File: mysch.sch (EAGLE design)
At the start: 41 parts, among them IC1 CY8C4247LQI-BL483, IC2 74HC595N, J1 FTSH-105-01-L-DV-K, J2 22-23-2051, Q1 RFD3055LE, Y2 ECS-240-8-36CKM-TR

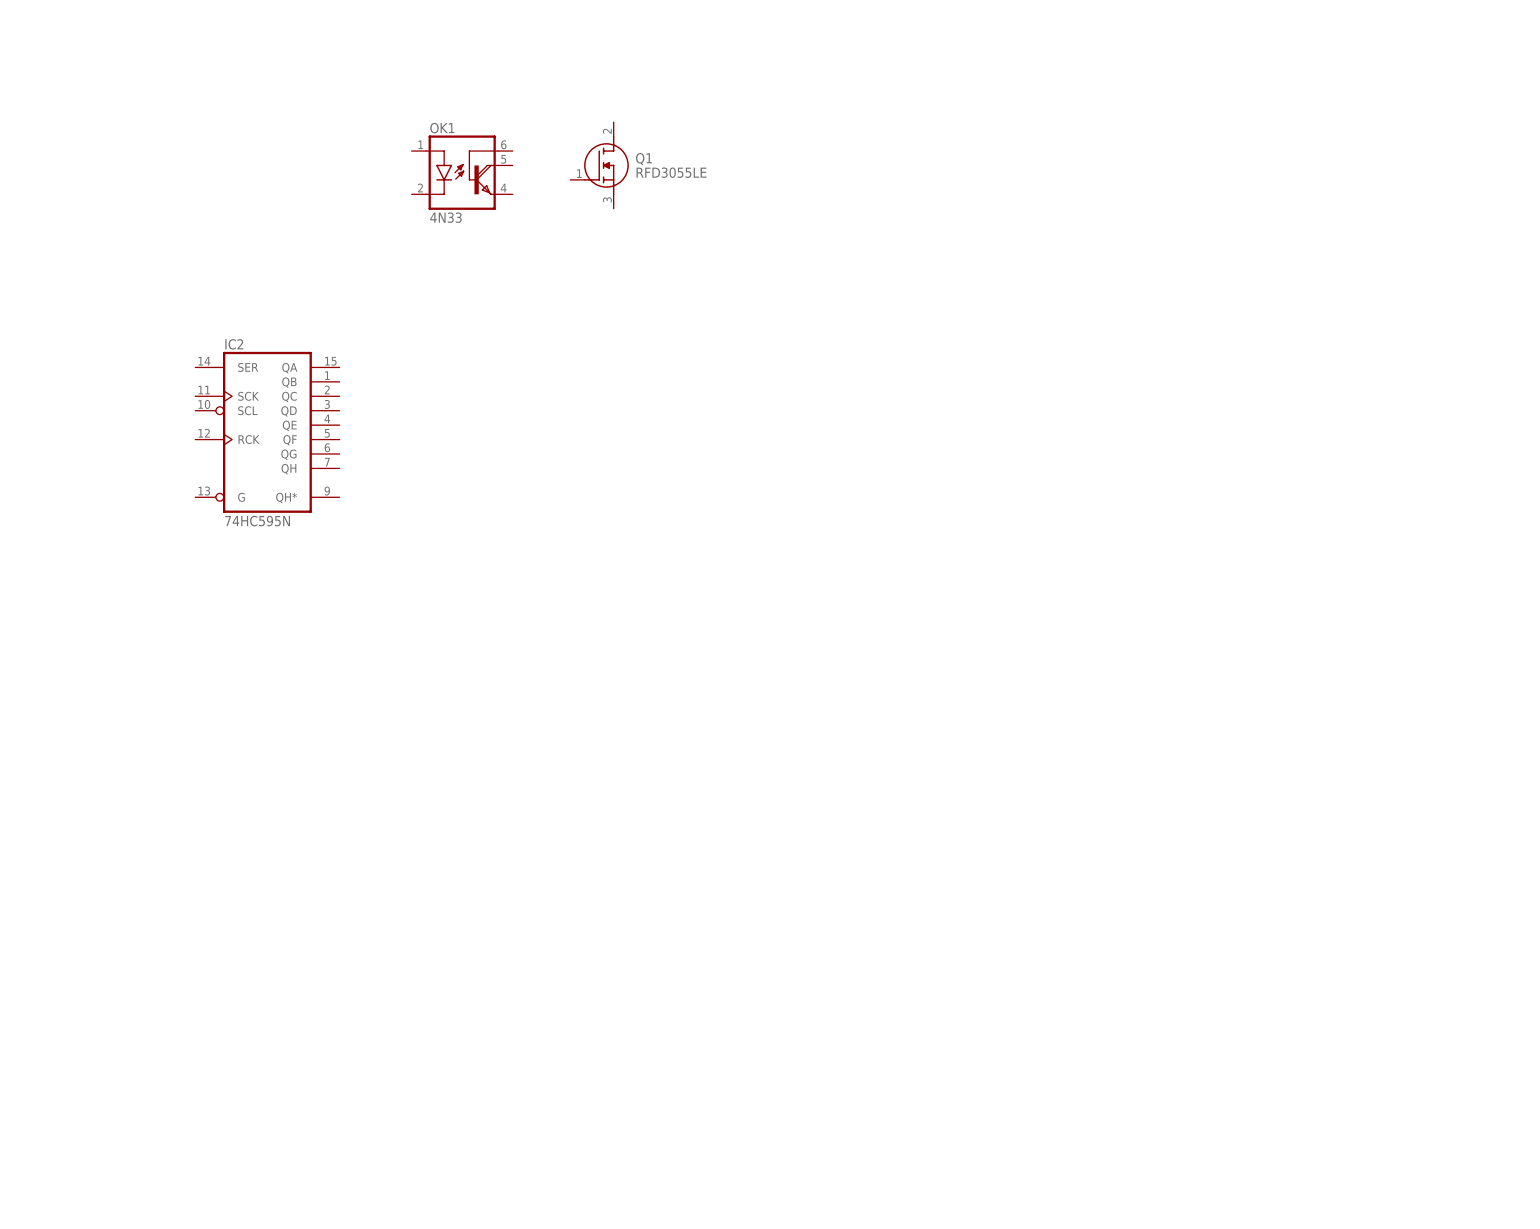
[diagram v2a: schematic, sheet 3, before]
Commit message: more on nmos circuit
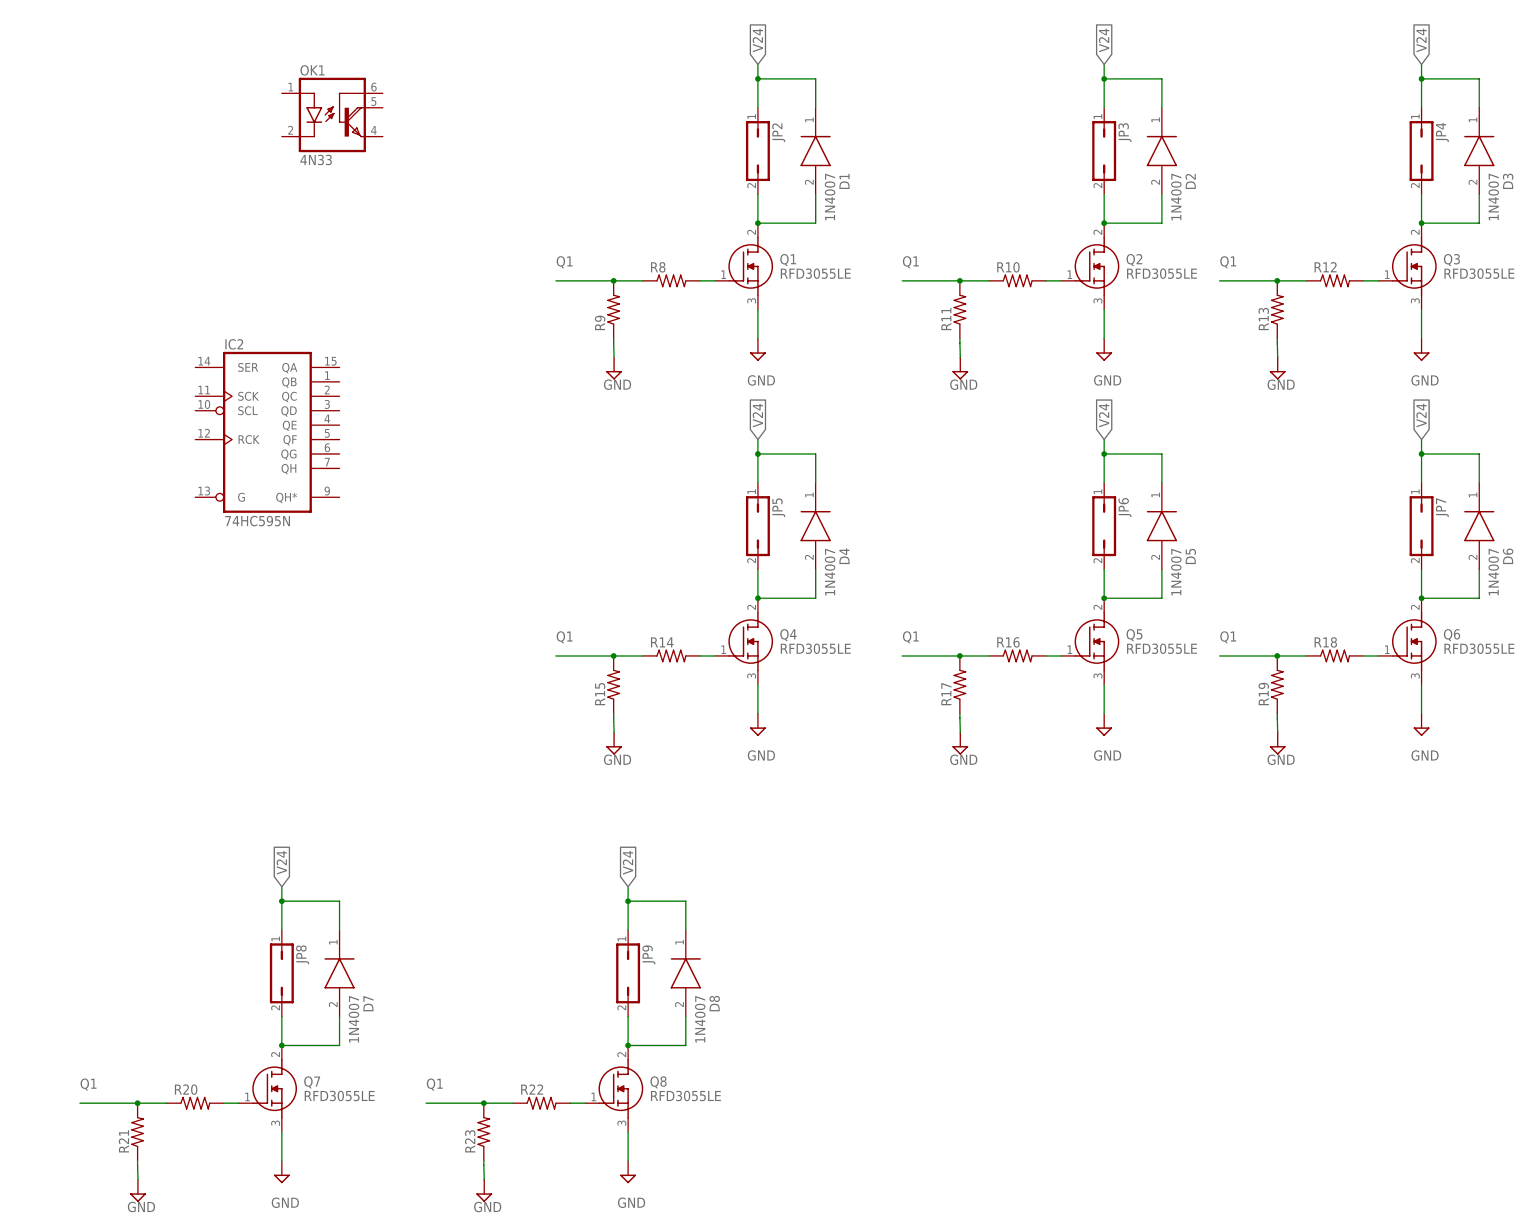
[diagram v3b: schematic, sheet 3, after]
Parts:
- removed SW1: (no value), adafruit:SWITCH_PUSHBUTTONC&K_KSS
- added D1, D2, D3, D4, D5, D6, D7, D8: 1N4007, SamacSys_Parts:1N4007
- added JP3, JP4, JP5, JP6, JP7, JP8, JP9: (no value), jumper:JP1Q
- added Q2, Q3, Q4, Q5, Q6, Q7, Q8: RFD3055LE, SamacSys_Parts:RFD3055LE
- added R10, R11, R12, R13, R14, R15, R16, R17, R18, R19, R20, R21, R22, R23, R8, R9: (no value), rcl:R-US_R0805
- JP2: device pinhead:PINHD-1X2 -> jumper:JP1Q
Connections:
- removed net UART_RX: BT_SLAVE.UART-RX, JP2.2
- removed net UART_TX: BT_SLAVE.!UART-CTS, JP2.1
- new net N$11: D3.A, JP4.2, Q3.D
- new net N$12: Q3.G, R12.2
- new net N$13: D4.A, JP5.2, Q4.D
- new net N$14: Q4.G, R14.2
- new net N$15: D5.A, JP6.2, Q5.D
- new net N$16: Q5.G, R16.2
- new net N$17: D6.A, JP7.2, Q6.D
- new net N$18: Q6.G, R18.2
- new net N$19: D7.A, JP8.2, Q7.D
- new net N$20: Q7.G, R20.2
- new net N$21: D8.A, JP9.2, Q8.D
- new net N$22: Q8.G, R22.2
- new net N$6: Q1.G, R8.2
- new net N$7: D1.A, JP2.2, Q1.D
- new net N$8: D2.A, JP3.2, Q2.D
- new net N$9: Q2.G, R10.2
- new net Q1: R10.1, R11.2, R12.1, R13.2, R14.1, R15.2, R16.1, R17.2, R18.1, R19.2, R20.1, R21.2, R22.1, R23.2, R8.1, R9.2
- new net V24: D1.K, D2.K, D3.K, D4.K, D5.K, D6.K, D7.K, D8.K, JP2.1, JP3.1, JP4.1, JP5.1, JP6.1, JP7.1, JP8.1, JP9.1
- net +3V3: no longer SW1.P$2
- net GND: now also Q1.S, Q2.S, Q3.S, Q4.S, Q5.S, Q6.S, Q7.S, Q8.S, R11.1, R13.1, R15.1, R17.1, R19.1, R21.1, R23.1, R9.1
- net N$1: no longer SW1.P$1
- net P1.4: now also BT_SLAVE.!UART-CTS
- net P1.5: now also BT_SLAVE.UART-RX
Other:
- moved on the sheet: OK1, Q1

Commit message: added shift register and nmos switch circuit
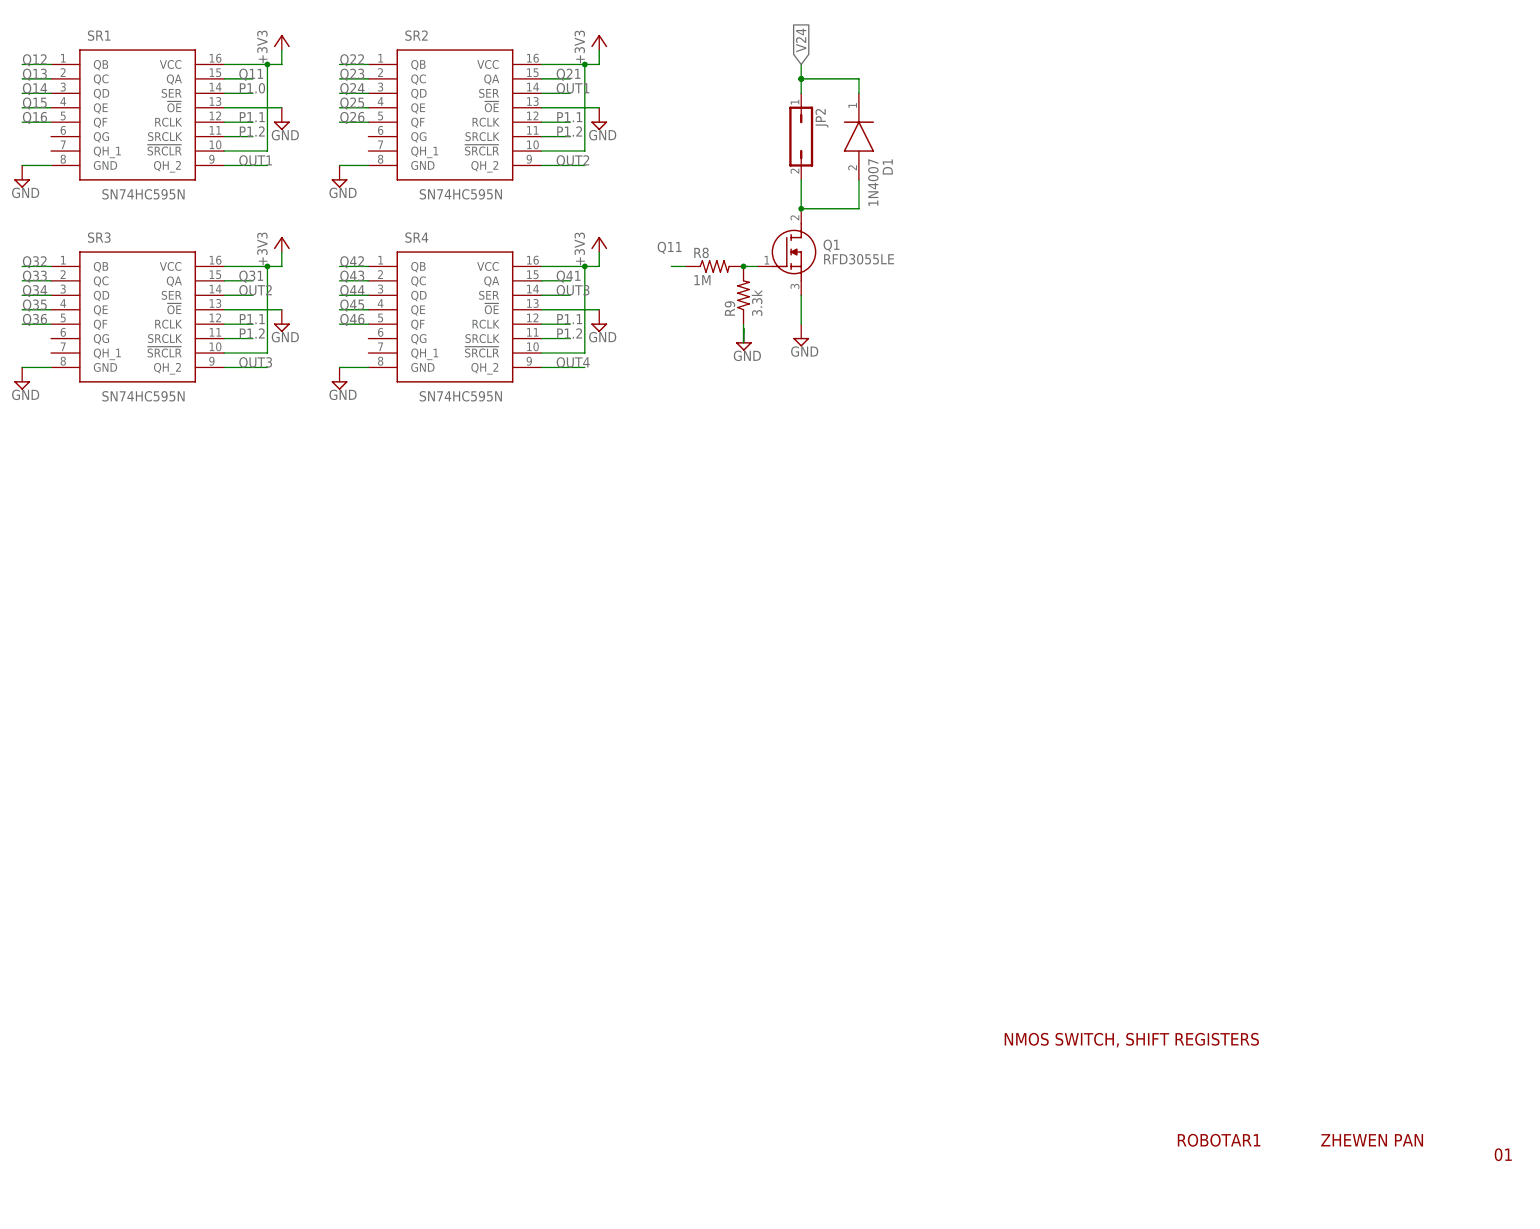
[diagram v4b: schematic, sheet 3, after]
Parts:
- removed D4, D5, D6, D7, D8: 1N4007, SamacSys_Parts:1N4007
- removed IC2: 74HC595N, 74xx-eu:74HC595N
- removed JP1: (no value), pinhead:PINHD-1X2
- removed JP3, JP4, JP5, JP6, JP7, JP8, JP9: (no value), jumper:JP1Q
- removed OK1: 4N33, optocoupler:4N33
- removed Q2, Q3, Q4, Q5, Q6, Q7, Q8: RFD3055LE, SamacSys_Parts:RFD3055LE
- removed R10, R11, R12, R13, R14, R15, R16, R17, R18, R19, R20, R21, R22, R23: (no value), rcl:R-US_R0805
- added C20, C21: (no value), rcl:C-USC0805
- added SR1, SR2, SR3, SR4: SN74HC595N, SamacSys_Parts:SN74HC595N
- added Y1: ECS-.327-12.5-34B-TR, SamacSys_Parts:ECS-.327-12.5-34B-TR
- D2, D3: value 1N4007 -> B5819XP-TP; device SamacSys_Parts:1N4007 -> SamacSys_Parts:B5819XP-TP
- R4: value 470 -> 4.7k
- R8: value (none) -> 1M
- R9: value (none) -> 3.3k
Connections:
- removed net KEY: JP1.1, R4.1
- removed net N$12: Q3.G, R12.2
- removed net N$13: D4.A, JP5.2, Q4.D
- removed net N$14: Q4.G, R14.2
- removed net N$15: D5.A, JP6.2, Q5.D
- removed net N$16: Q5.G, R16.2
- removed net N$17: D6.A, JP7.2, Q6.D
- removed net N$18: Q6.G, R18.2
- removed net N$19: D7.A, JP8.2, Q7.D
- removed net N$20: Q7.G, R20.2
- removed net N$21: D8.A, JP9.2, Q8.D
- removed net N$22: Q8.G, R22.2
- removed net N$8: D2.A, JP3.2, Q2.D
- removed net N$9: Q2.G, R10.2
- removed net Q1: R10.1, R11.2, R12.1, R13.2, R14.1, R15.2, R16.1, R17.2, R18.1, R19.2, R20.1, R21.2, R22.1, R23.2, R8.1, R9.2
- new net OUT1: SR1.QH_2, SR2.SER
- new net OUT2: SR2.QH_2, SR3.SER
- new net OUT3: SR3.QH_2, SR4.SER
- new net OUT4: SR4.QH_2
- new net Q11: R8.1, SR1.QA
- new net Q12: SR1.QB
- new net Q13: SR1.QC
- new net Q14: SR1.QD
- new net Q15: SR1.QE
- new net Q16: SR1.QF
- new net Q21: SR2.QA
- new net Q22: SR2.QB
- new net Q23: SR2.QC
- new net Q24: SR2.QD
- new net Q25: SR2.QE
- new net Q26: SR2.QF
- new net Q31: SR3.QA
- new net Q32: SR3.QB
- new net Q33: SR3.QC
- new net Q34: SR3.QD
- new net Q35: SR3.QE
- new net Q36: SR3.QF
- new net Q41: SR4.QA
- new net Q42: SR4.QB
- new net Q43: SR4.QC
- new net Q44: SR4.QD
- new net Q45: SR4.QE
- new net Q46: SR4.QF
- net +3V3: now also R3.2, R4.2, SR1.!SRCLR, SR1.VCC, SR2.!SRCLR, SR2.VCC, SR3.!SRCLR, SR3.VCC, SR4.!SRCLR, SR4.VCC
- net GND: now also C20.1, C21.1, SR1.!OE, SR1.GND, SR2.!OE, SR2.GND, SR3.!OE, SR3.GND, SR4.!OE, SR4.GND; no longer Q2.S, Q3.S, Q4.S, Q5.S, Q6.S, Q7.S, Q8.S, R11.1, R13.1, R15.1, R17.1, R19.1, R21.1, R23.1, R3.2
- net N$1: now also BT_SLAVE.UART-TX, D2.-; no longer BT_SLAVE.PIO[11], R3.1, R4.2
- net N$11: now also BT_SLAVE.UART-RX, D3.+, R4.1; no longer D3.A, JP4.2, Q3.D
- net N$6: now also R9.2
- net P1.0: now also SR1.SER
- net P1.1: now also SR1.RCLK, SR2.RCLK, SR3.RCLK, SR4.RCLK
- net P1.2: now also SR1.SRCLK, SR2.SRCLK, SR3.SRCLK, SR4.SRCLK
- net P1.4: now also D2.+, R3.1; no longer BT_SLAVE.!UART-CTS
- net P1.5: now also D3.-; no longer BT_SLAVE.UART-RX
- net P1.6: now also BT_SLAVE.PIO[11]
- net P6.0: now also C21.2, Y1.1
- net P6.1: now also C20.2, Y1.2
- net V24: no longer D2.K, D3.K, D4.K, D5.K, D6.K, D7.K, D8.K, JP3.1, JP4.1, JP5.1, JP6.1, JP7.1, JP8.1, JP9.1
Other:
- note added: "01"
- note added: "CY8C4247LQI-BL483"
- note added: "NMOS SWITCH, SHIFT REGISTERS"
- note added: "ROBOTA1"
- note added: "ROBOTAR1"
- note added: "ZHEWEN PAN"
- moved on the sheet: D1, JP2, LED1, LED2, Q1, R1, R2, R3, R4, R8, R9
